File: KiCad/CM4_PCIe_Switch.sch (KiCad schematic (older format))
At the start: 6 parts

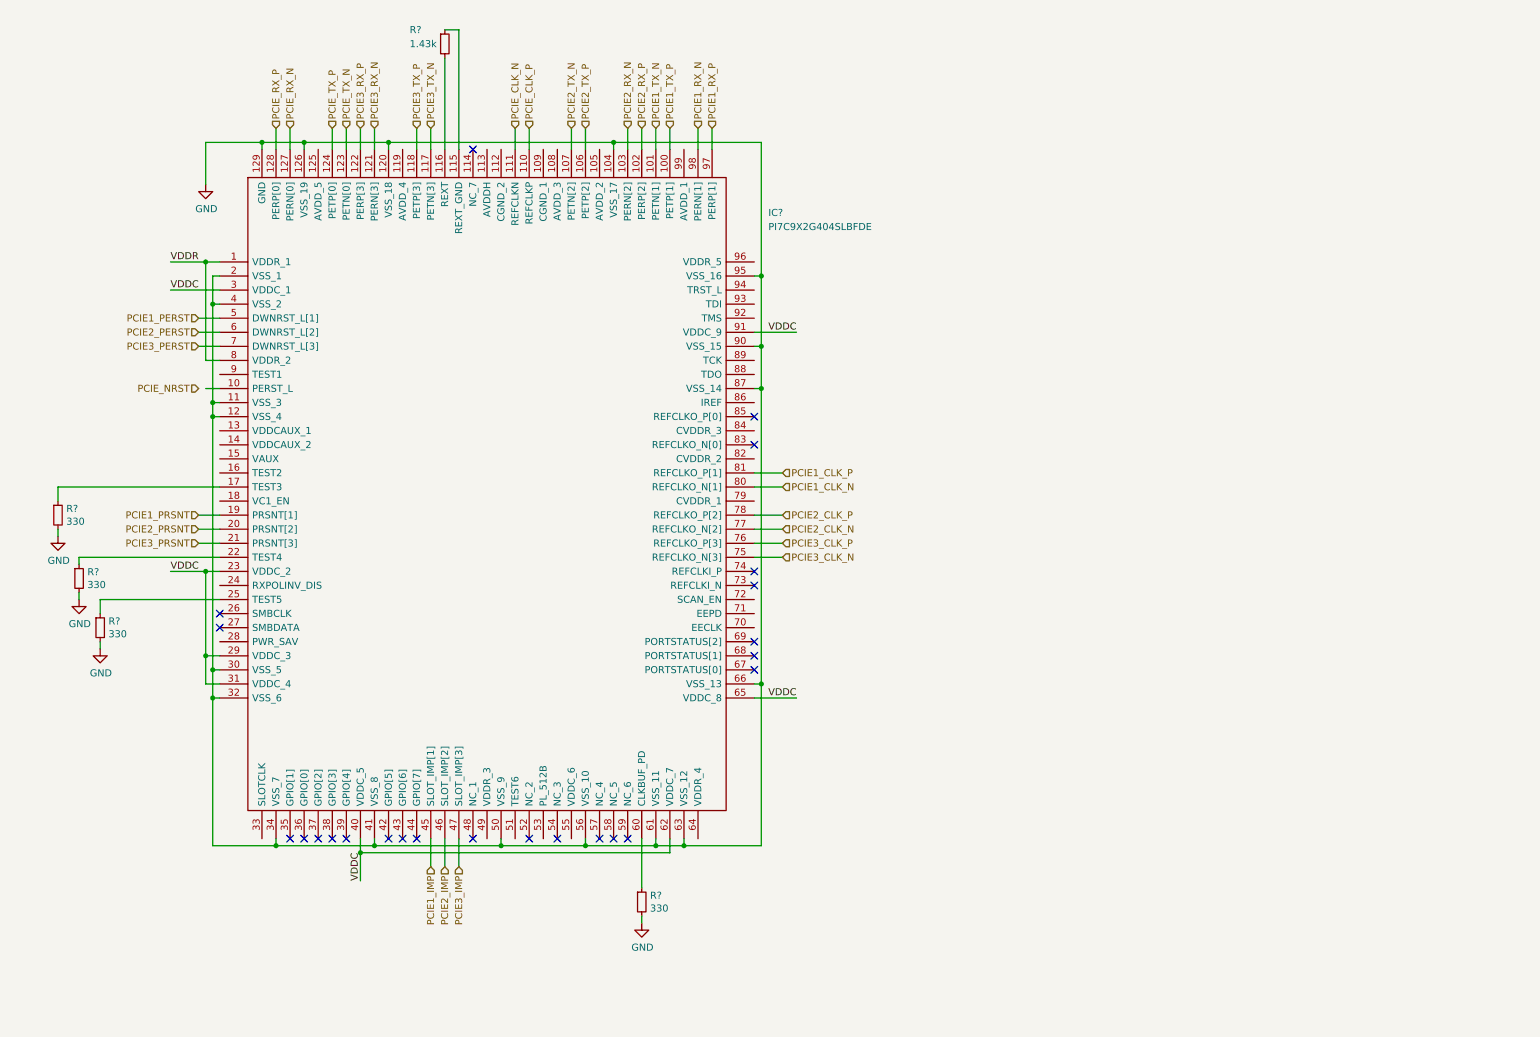
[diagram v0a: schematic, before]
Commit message: Lotsa changes
Added new footprints:
PCIe x1, TO-252 tab, SOT95, SOP50, SON50, Hirose FH-12-22S, 2.54mm 2x02 and 2x05 headers
Added new models:
Hirose FH-12-22S, FSUSB42MUX, MIC2019YM6-TR, TPS6206
Re-did ATX connector symbol wiring
Begun wiring PI7C PCI-e switch
Wired USB2517 hub
Begun adding MIC2019YM6 current limiters.
Added TODO lists to each page to help new contributors
Begun placing PCB footprints and descriptors
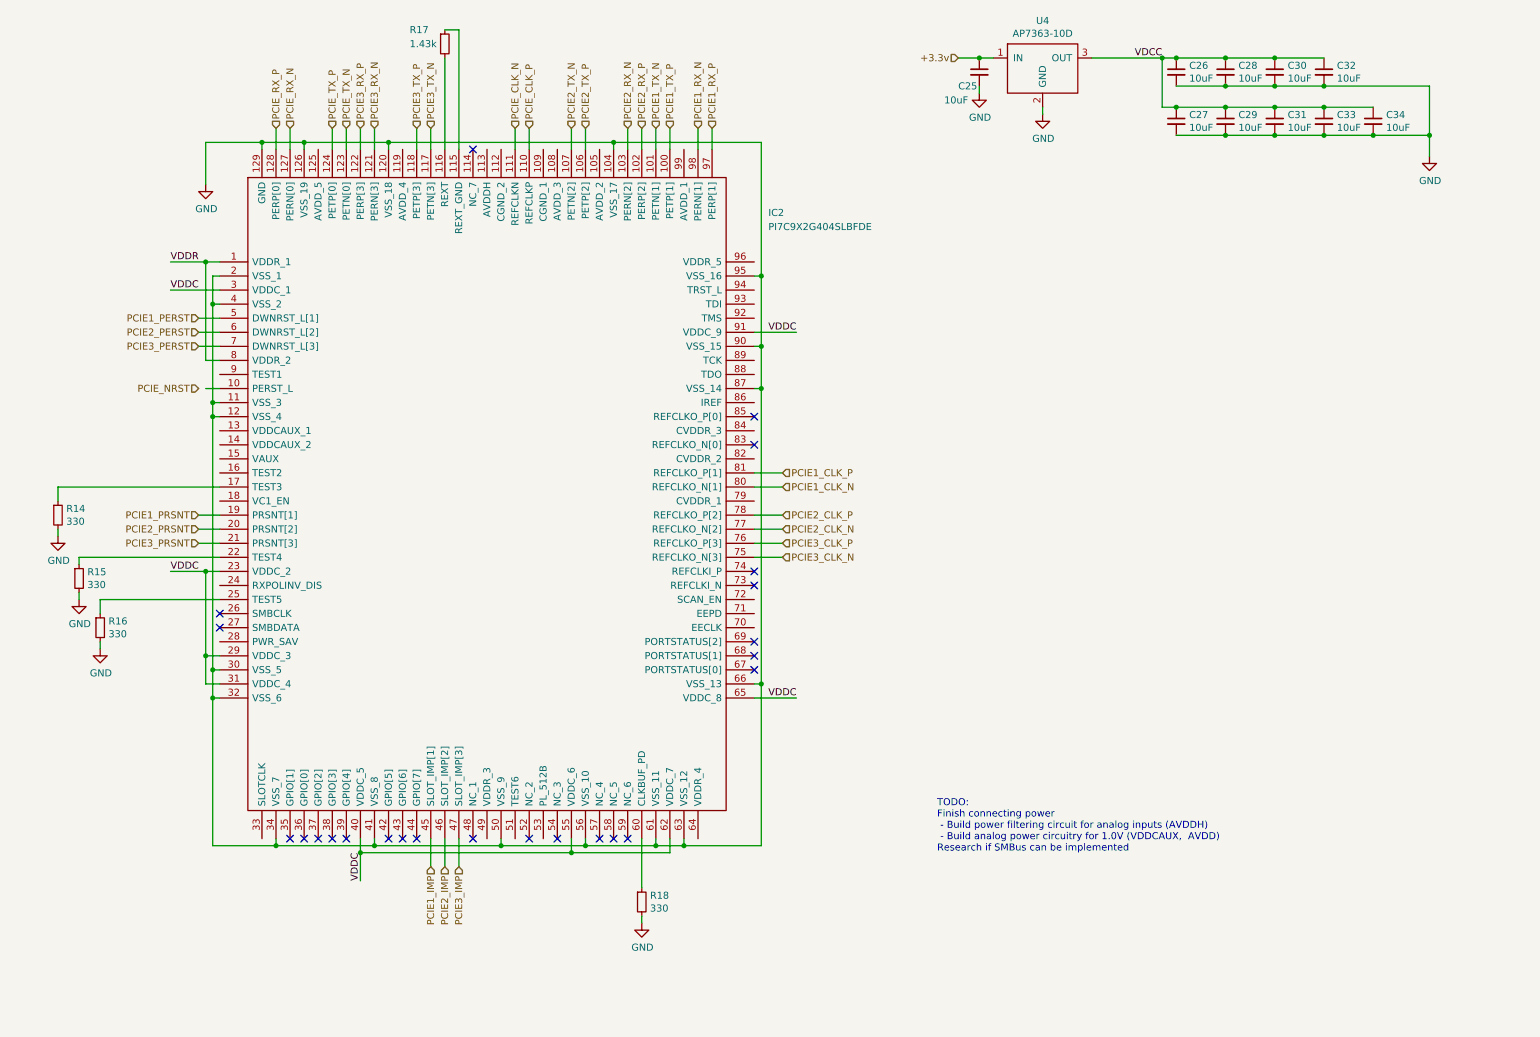
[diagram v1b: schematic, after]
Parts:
- added C25, C26, C27, C28, C29, C30, C31, C32, C33, C34: 10uF, symbol Device:C_Small
- added U4: AP7363-10D, CM4_MATX:TO-252-3_TabPin2, symbol CM4_MATX:AP7363-10D
- gave numbers to parts that had none: 6
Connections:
- net GND: now also C25.2, C26.2, C27.2, C28.2, C29.2, C30.2, C31.2, C32.2, C33.2, C34.2, U4.2 (GND)
- net VDDC: now also IC2.55 (VDDC_6)
- new net +3.3v: C25.1, U4.1 (IN)
- new net VDCC: C26.1, C27.1, C28.1, C29.1, C30.1, C31.1, C32.1, C33.1, C34.1, U4.3 (OUT)
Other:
- note added: "TODO:\nFinish connecting power\n - Build power filtering circuit for analog inputs (AVDDH)\n - Build analog power circuitry for 1.0V (VDDCAUX, AVDD)\nResearch if SMBus can be implemented"

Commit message: Many, many changes...
Added a bunch of new footprints and a couple of new symbols.
Added the other side of the CM4 connector and wired its features.
Added some more detailed models for a fair few components.
Added a new schematic to handle power for USB ports.
Updated the PCB with the new components and moved some around to populate the rear IO panel.
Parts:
- IC2: footprint QFP40P1600X1600X160-129N -> CM4_MATX:QFP40P1600X1600X160-129N
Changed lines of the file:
@@
 $Descr A4 11693 8268
 encoding utf-8
-Sheet 5 6
+Sheet 5 8
 Title "CM4_MATX: PCIe Switch"
 Date "2020-11-19"
@@
 F 0 "IC2" H 5800 2650 50  0000 L CNN
 F 1 "PI7C9X2G404SLBFDE" H 5800 2550 50  0000 L CNN
-F 2 "QFP40P1600X1600X160-129N" H 5550 2900 50  0001 L CNN
+F 2 "CM4_MATX:QFP40P1600X1600X160-129N" H 5550 2900 50  0001 L CNN
 F 3 "https://www.mouser.co.uk/datasheet/2/115/PI7C9X2G404SL-1140655.pdf" H 5550 2800 50  0001 L CNN
 F 4 "PCI Interface IC 4 port 4 lane PCIe 2.0 Packet Switch" H 5550 2700 50  0001 L CNN "Description"

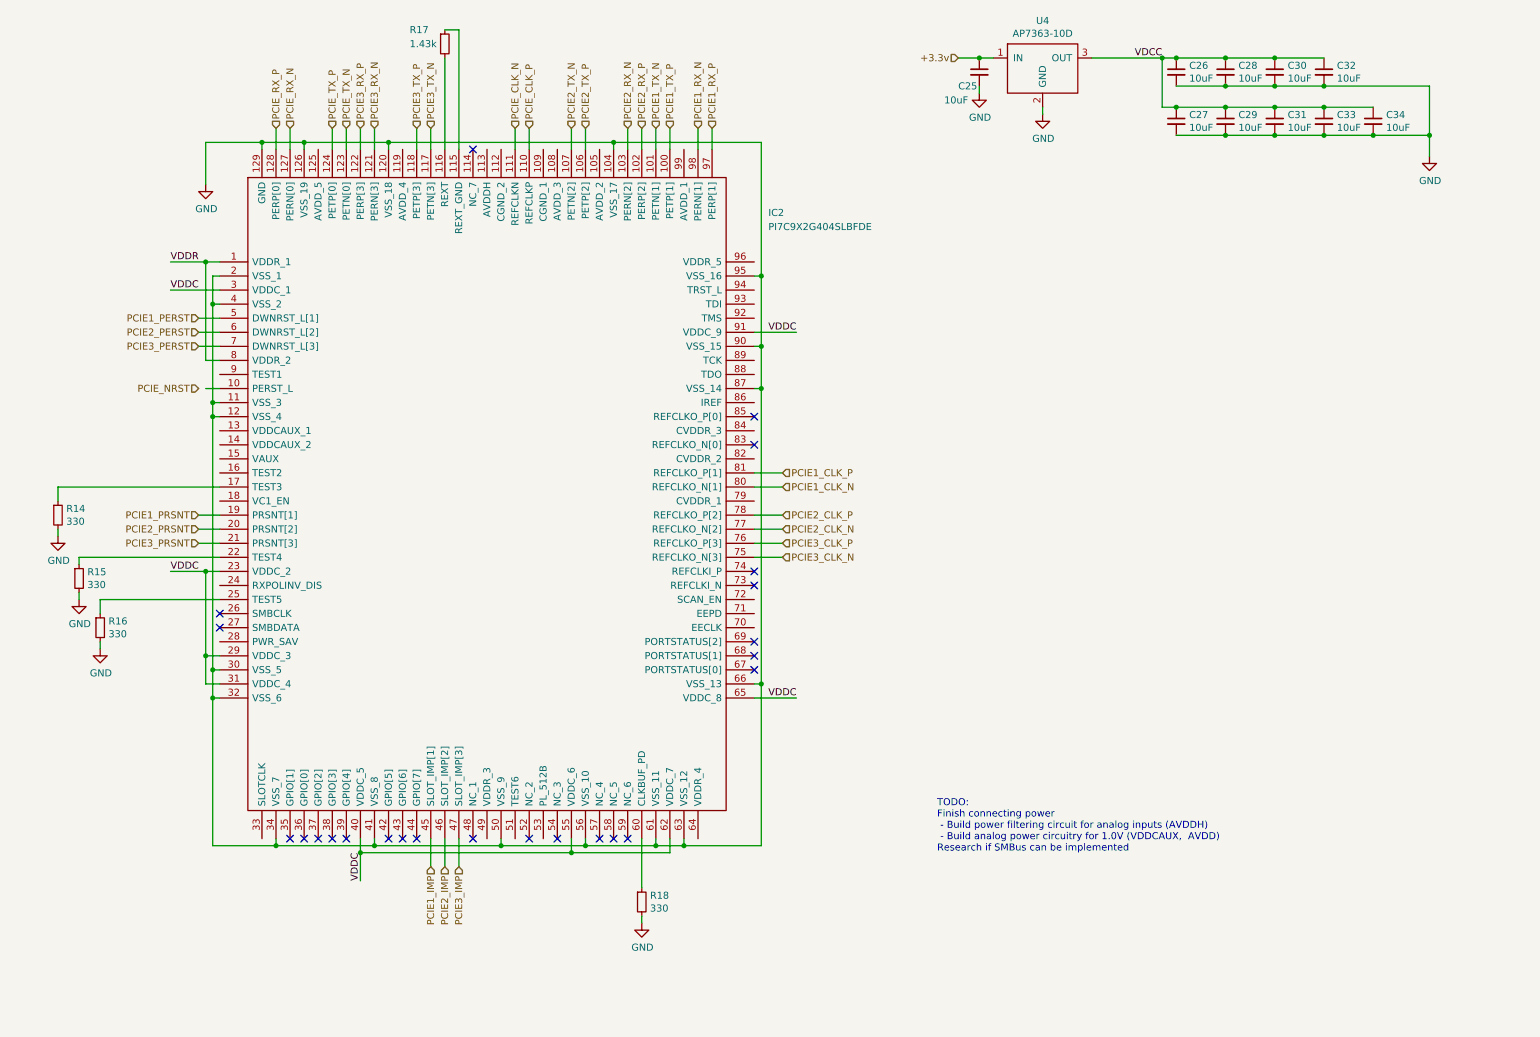
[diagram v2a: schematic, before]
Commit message: Small changes to PCIe, USB Schematics and board layout, legend for GPIO pins.
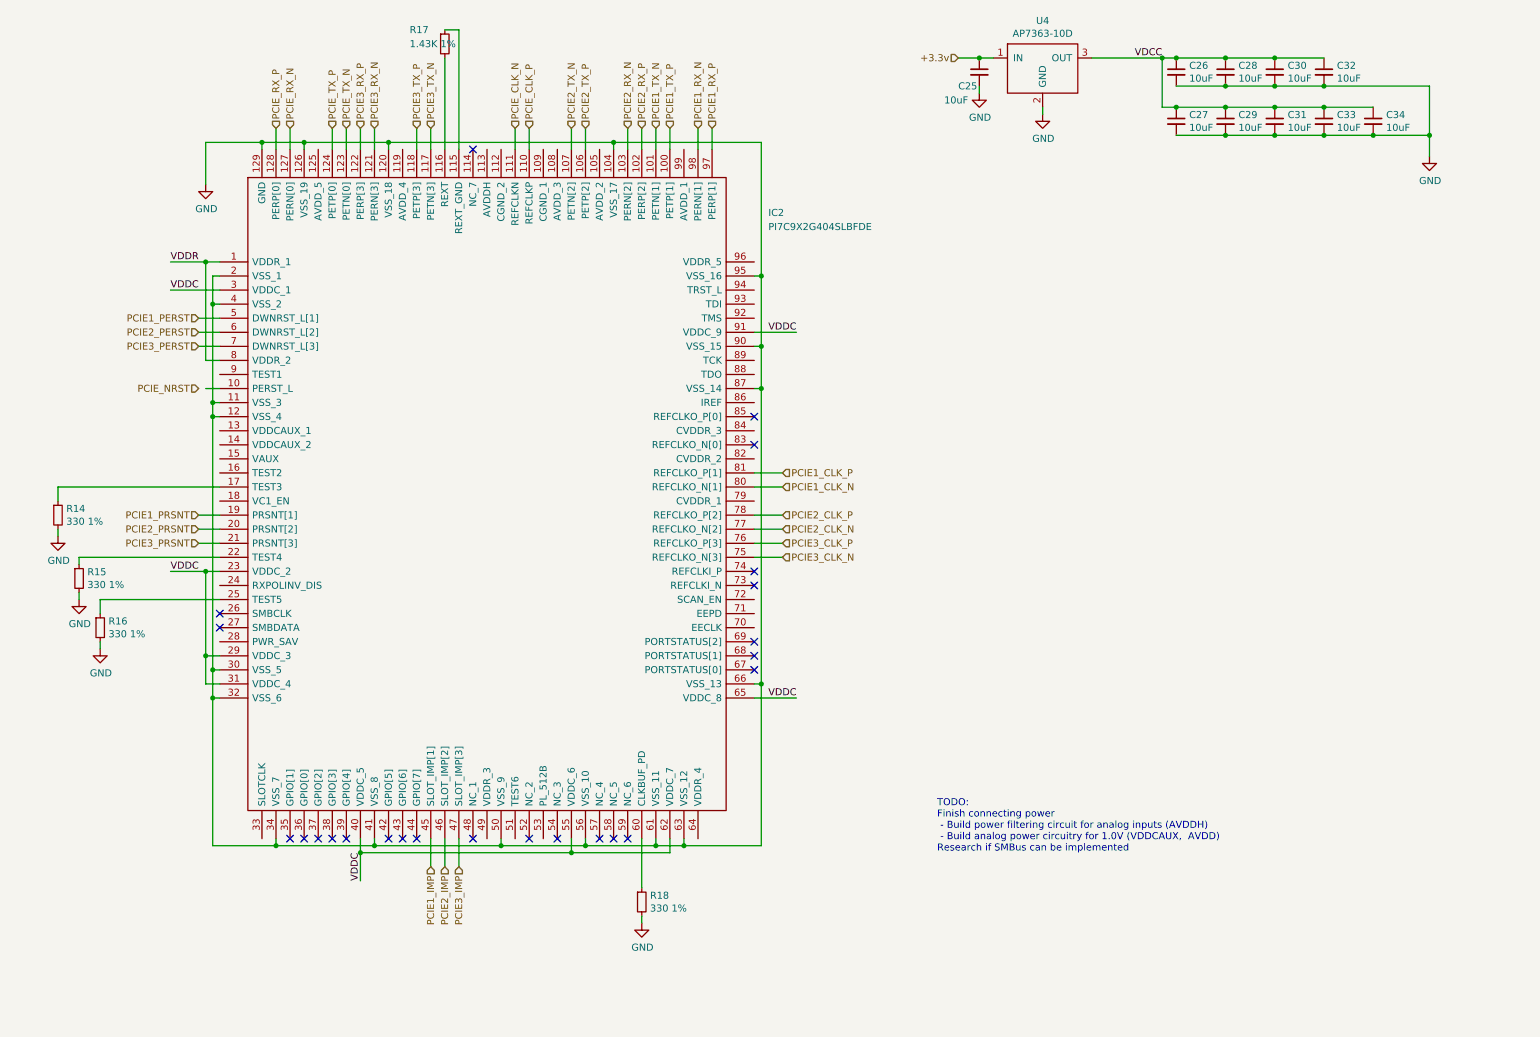
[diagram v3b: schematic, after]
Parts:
- R14, R15, R16, R18: value 330 -> 330 1%
- R17: value 1.43k -> 1.43K 1%
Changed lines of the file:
@@
 $Descr A4 11693 8268
 encoding utf-8
-Sheet 5 8
+Sheet 5 10
 Title "CM4_MATX: PCIe Switch"
-Date "2020-11-19"
+Date "2020-11-27"
 Rev "0.1"
-Comp "Oliver Møller/TheGuyDanish"
+Comp "CM4_MATX Contributors"
 Comment1 "https://github.com/theguydanish/CM4_MATX"
 Comment2 ""
@@
 P 750 4100
 F 0 "R14" H 809 4146 50  0000 L CNN
-F 1 "330" H 809 4055 50  0000 L CNN
+F 1 "330 1%" H 809 4055 50  0000 L CNN
 F 2 "" H 750 4100 50  0001 C CNN
 F 3 "~" H 750 4100 50  0001 C CNN
@@
 P 900 4550
 F 0 "R15" H 959 4596 50  0000 L CNN
-F 1 "330" H 959 4505 50  0000 L CNN
+F 1 "330 1%" H 959 4505 50  0000 L CNN
 F 2 "" H 900 4550 50  0001 C CNN
 F 3 "~" H 900 4550 50  0001 C CNN
@@
 P 1050 4900
 F 0 "R16" H 1109 4946 50  0000 L CNN
-F 1 "330" H 1109 4855 50  0000 L CNN
+F 1 "330 1%" H 1109 4855 50  0000 L CNN
 F 2 "" H 1050 4900 50  0001 C CNN
 F 3 "~" H 1050 4900 50  0001 C CNN
@@
 P 4900 6850
 F 0 "R18" H 4959 6896 50  0000 L CNN
-F 1 "330" H 4959 6805 50  0000 L CNN
+F 1 "330 1%" H 4959 6805 50  0000 L CNN
 F 2 "" H 4900 6850 50  0001 C CNN
 F 3 "~" H 4900 6850 50  0001 C CNN
@@
 P 3500 750
 F 0 "R17" H 3250 850 50  0000 L CNN
-F 1 "1.43k" H 3250 750 50  0000 L CNN
+F 1 "1.43K 1%" H 3250 750 50  0000 L CNN
 F 2 "" H 3500 750 50  0001 C CNN
 F 3 "~" H 3500 750 50  0001 C CNN
